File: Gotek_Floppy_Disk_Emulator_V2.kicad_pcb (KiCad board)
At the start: 2 copper layers, 90 x 60 mm, 66 parts, among them J1 Power Connector, J2 OLED Display 0.91" Module, J3 USB_A, J5 Programming Connector, J6 Floppy Data Connector, Q1 MMBT2222, Q2 BSS123, Q3 BSS123, Q4 BSS123, Q5 BSS123, Q6 BSS123, Q7 BSS123, SW1 KY040 Rotary Encoder Module, SW2 DIP Switch, U1 AMS1117-3.3, U2 STM32F105RBTx, U3 STMPS2141, U4 74HCT04, Y1 8MHz

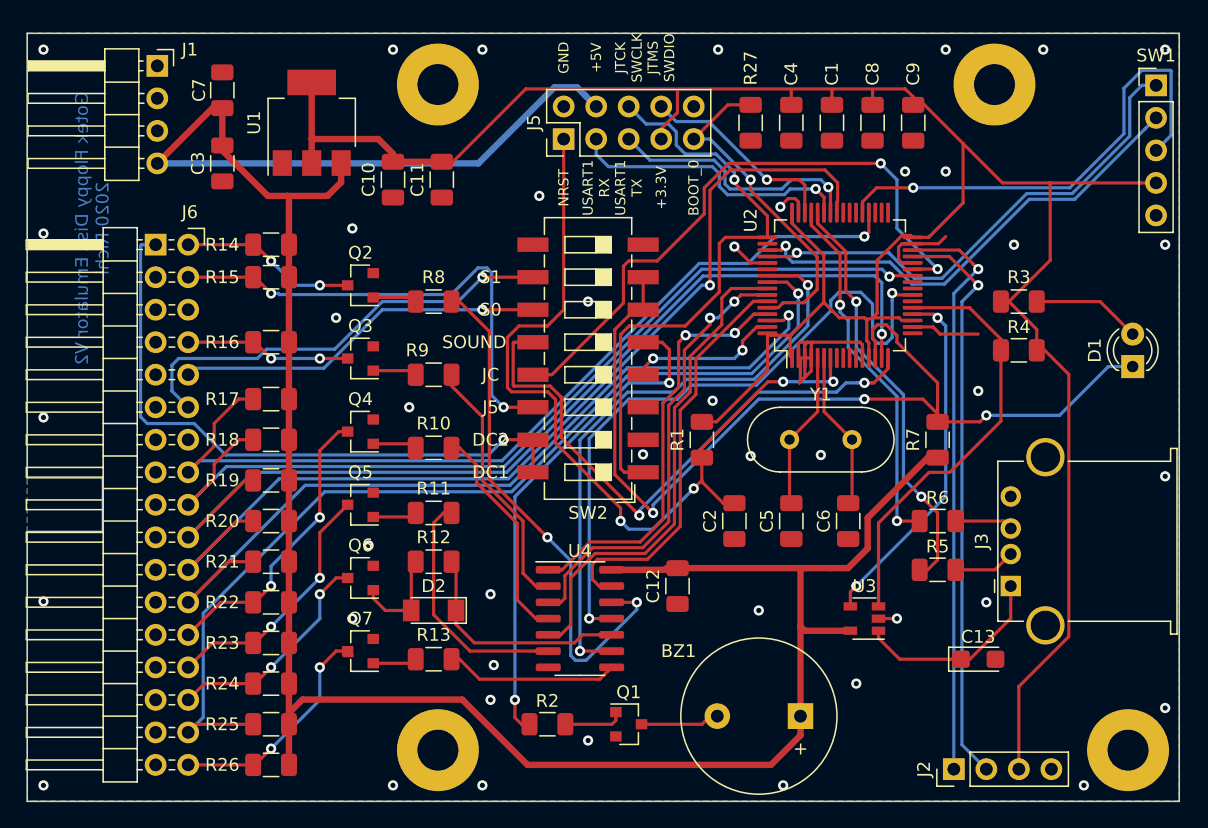
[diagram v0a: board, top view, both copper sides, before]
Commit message: Production files generated
Some parts were exchanged for SMD mounted. For production generation was used Bouni/kicad-jlcpcb-tools plugin.
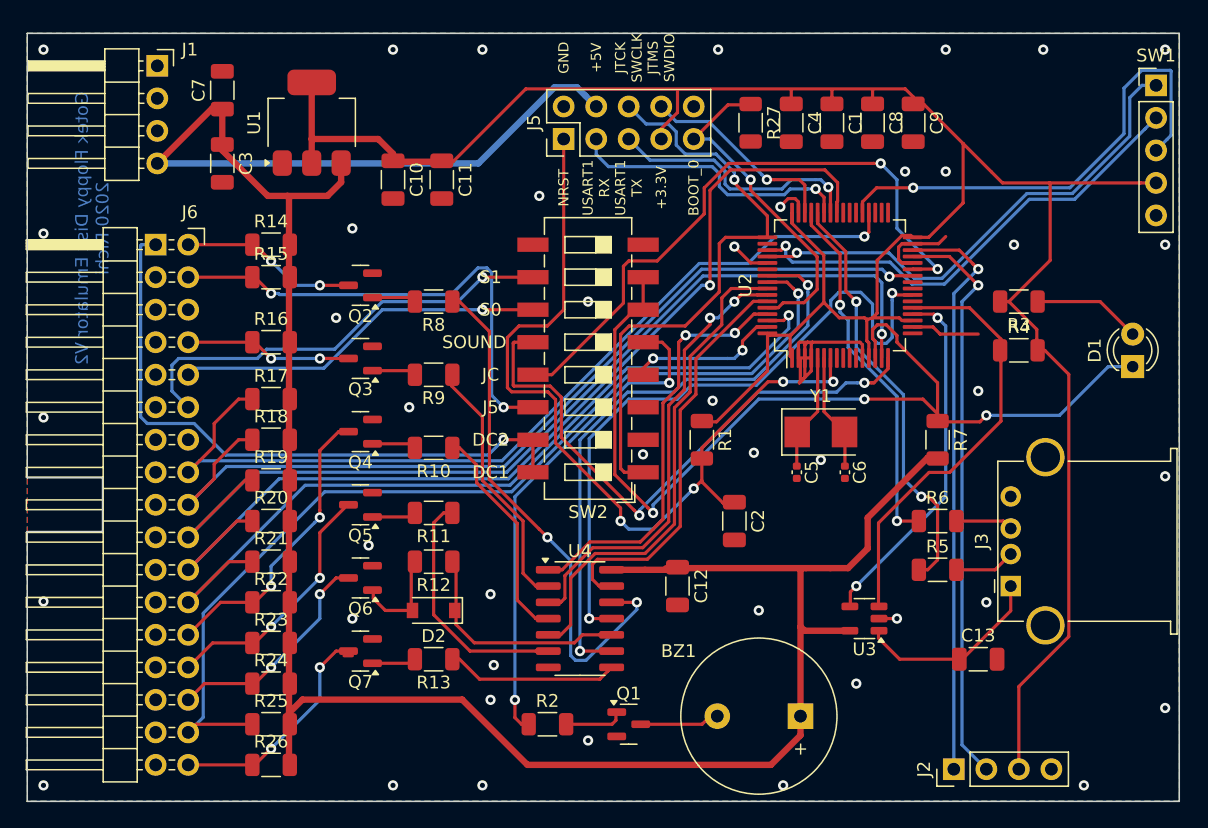
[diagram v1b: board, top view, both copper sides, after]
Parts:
- removed REF** (x4): MountingHole_3.2mm_M3_Pad, Gotek_Floppy_Disk_Emulator_V2:MountingHole_3.2mm_M3_Pad
- C1, C10, C11, C12, C2, C3, C4, C7, C8, C9: footprint Gotek_Floppy_Disk_Emulator_V2:C_1206_3216Metric -> Capacitor_SMD:C_1206_3216Metric
- C13: footprint Gotek_Floppy_Disk_Emulator_V2:CP_EIA-3216-18_Kemet-A -> Capacitor_SMD:C_1206_3216Metric
- C5, C6: footprint Gotek_Floppy_Disk_Emulator_V2:C_1206_3216Metric -> Capacitor_SMD:C_0402_1005Metric
- D1: footprint Gotek_Floppy_Disk_Emulator_V2:LED_D3.0mm -> LED_THT:LED_D3.0mm
- D2: footprint Gotek_Floppy_Disk_Emulator_V2:D_MiniMELF -> Diode_SMD:D_SOD-123
- J5: footprint Gotek_Floppy_Disk_Emulator_V2:PinHeader_2x05_P2.54mm_Vertical -> Connector_PinHeader_2.54mm:PinHeader_2x05_P2.54mm_Vertical
- Q1, Q2, Q3, Q4, Q5, Q6, Q7: footprint Gotek_Floppy_Disk_Emulator_V2:SOT-23 -> Package_TO_SOT_SMD:SOT-23
- R1, R10, R11, R12, R13, R14, R15, R16, R17, R18, R19, R2, R20, R21, R22, R23, R24, R25, R26, R27, R3, R4, R5, R6, R7, R8, R9: footprint Gotek_Floppy_Disk_Emulator_V2:R_1206_3216Metric -> Resistor_SMD:R_1206_3216Metric
- SW1: footprint Gotek_Floppy_Disk_Emulator_V2:PinHeader_1x05_P2.54mm_Vertical -> Connector_PinHeader_2.54mm:PinHeader_1x05_P2.54mm_Vertical
- SW2: footprint Gotek_Floppy_Disk_Emulator_V2:SW_DIP_SPSTx08_Slide_6.7x21.88mm_W8.61mm_P2.54mm_LowProfile -> Button_Switch_SMD:SW_DIP_SPSTx08_Slide_6.7x21.88mm_W8.61mm_P2.54mm_LowProfile
- U1: footprint Gotek_Floppy_Disk_Emulator_V2:SOT-223-3_TabPin2 -> Package_TO_SOT_SMD:SOT-223-3_TabPin2
- U3: footprint Gotek_Floppy_Disk_Emulator_V2:SOT-23-5 -> Package_TO_SOT_SMD:SOT-23-5
- U4: footprint Gotek_Floppy_Disk_Emulator_V2:SOIC-14_3.9x8.7mm_P1.27mm -> Package_SO:SOIC-14_3.9x8.7mm_P1.27mm
- Y1: footprint Gotek_Floppy_Disk_Emulator_V2:Crystal_HC49-4H_Vertical -> Crystal:Crystal_SMD_5032-2Pin_5.0x3.2mm
- moved C5 3.83 mm to (142.0, 90.2)
- moved C6 3.82 mm to (145.8, 90.2)
- moved Y1 2.52 mm to (143.9, 87.0)
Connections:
- J1 pad 1: Net-(J1-Pad1) -> unconnected-(J1-Pin_1-Pad1)
- J5 pad 10: Net-(J5-Pad10) -> unconnected-(J5-Pin_10-Pad10)
- J6 pad 14: Net-(J6-Pad14) -> unconnected-(J6-Pin_14-Pad14)
- J6 pad 6: Net-(J6-Pad6) -> unconnected-(J6-Pin_6-Pad6)
- SW2 pad 8: Net-(SW2-Pad8) -> unconnected-(SW2-Pad8)
- SW2 pad 9: Net-(SW2-Pad9) -> unconnected-(SW2-Pad9)
- U2 pad 10: Net-(U2-Pad10) -> unconnected-(U2-PC2-Pad10)
- U2 pad 11: Net-(U2-Pad11) -> unconnected-(U2-PC3-Pad11)
- U2 pad 17: Net-(U2-Pad17) -> unconnected-(U2-PA3-Pad17)
- U2 pad 22: Net-(U2-Pad22) -> unconnected-(U2-PA6-Pad22)
- U2 pad 24: Net-(U2-Pad24) -> unconnected-(U2-PC4-Pad24)
- U2 pad 25: Net-(U2-Pad25) -> unconnected-(U2-PC5-Pad25)
- U2 pad 33: Net-(U2-Pad33) -> unconnected-(U2-PB12-Pad33)
- U2 pad 34: Net-(U2-Pad34) -> unconnected-(U2-PB13-Pad34)
- U2 pad 35: Net-(U2-Pad35) -> unconnected-(U2-PB14-Pad35)
- U2 pad 38: Net-(U2-Pad38) -> unconnected-(U2-PC7-Pad38)
- U2 pad 39: Net-(U2-Pad39) -> unconnected-(U2-PC8-Pad39)
- U2 pad 40: Net-(U2-Pad40) -> unconnected-(U2-PC9-Pad40)
- U2 pad 50: Net-(U2-Pad50) -> unconnected-(U2-PA15-Pad50)
- U2 pad 54: Net-(U2-Pad54) -> unconnected-(U2-PD2-Pad54)
- U2 pad 8: Net-(U2-Pad8) -> unconnected-(U2-PC0-Pad8)
- U2 pad 9: Net-(U2-Pad9) -> unconnected-(U2-PC1-Pad9)
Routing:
- net Net-(U2-PD1): track 12.4 -> 9.97 mm
- net Net-(U2-PD0): track 12.3 -> 9.97 mm
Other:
- net class Default removed
- net class Power removed

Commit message: V2.1
Production files for JLCPCB excluding through hole parts and 8bit switch. Capacitors moved close to the voltage input pins of the MCU.
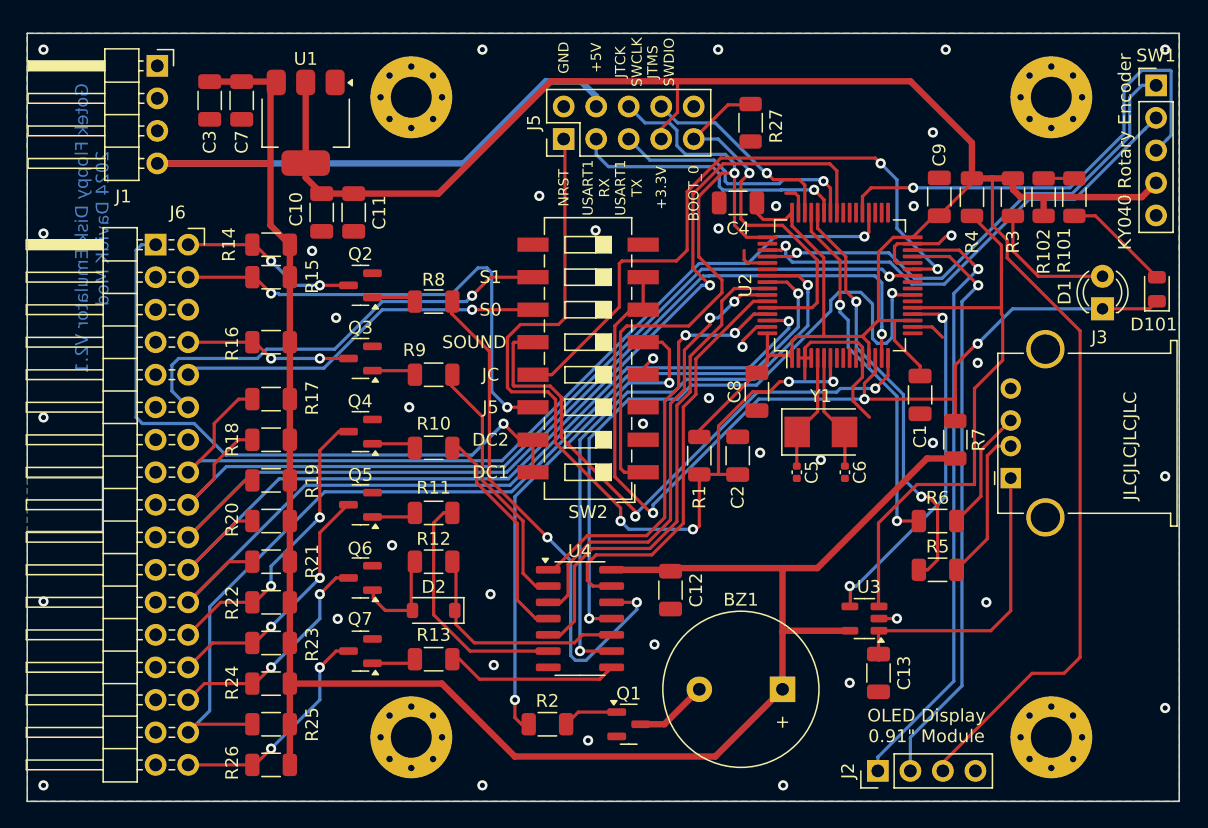
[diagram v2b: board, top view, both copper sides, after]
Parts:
- added D101: LED Green, LED_SMD:LED_0805_2012Metric, F.Cu at (170.2, 75.9)
- added H1: Hole1, MountingHole:MountingHole_3.2mm_M3_Pad_Via, F.Cu at (161.9, 60.9)
- added H2: Hole2, MountingHole:MountingHole_3.2mm_M3_Pad_Via, F.Cu at (161.9, 110.9)
- added H3: Hole3, MountingHole:MountingHole_3.2mm_M3_Pad_Via, F.Cu at (111.9, 60.9)
- added H4: Hole4, MountingHole:MountingHole_3.2mm_M3_Pad_Via, F.Cu at (111.9, 110.9)
- added R101: 1K, Resistor_SMD:R_1206_3216Metric, F.Cu at (163.7, 68.7)
- added R102: 1K, Resistor_SMD:R_1206_3216Metric, F.Cu at (161.3, 68.7)
- C13: value 4.7uF/16V -> 10uF/16V
- SW1: value KY040 Rotary Encoder Module -> KY040 Rotary Encoder
- moved C8 22.9 mm to (138.9, 83.9)
- moved C1 22.3 mm to (151.7, 84.1)
- moved R4 12.5 mm to (155.7, 68.7), turned to 90 degrees
- moved J3 8.44 mm to (158.8, 90.6)
- moved R3 8.17 mm to (158.9, 68.7), turned to 90 degrees
- moved C13 7.86 mm to (148.4, 105.8), turned to -90 degrees
- moved C4 7.52 mm to (137.4, 69.1), turned to 180 degrees
- moved C11 7.34 mm to (107.4, 69.9)
- moved C9 6.13 mm to (153.2, 68.6), turned to 90 degrees
- moved C10 6.13 mm to (104.9, 69.9)
- moved J2 5.94 mm to (148.4, 113.5)
- moved C2 5.11 mm to (137.4, 88.9), turned to 90 degrees
- moved D1 5.09 mm to (165.9, 77.4)
- moved C3 5.01 mm to (96.2, 61.1)
- moved BZ1 2.52 mm to (140.9, 107.1)
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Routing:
- net +3V3: track 192.4 -> 207.1 mm
- net GNDD: track 48.1 -> 35.1 mm, vias 45 -> 40
- net Net-(U2-PA5): track 33.7 -> 45.1 mm
- net Net-(D101-A): track 0.00 -> 8.44 mm
- net Net-(J3-VBUS): track 15.1 -> 23.2 mm
- net Net-(J3-D-): track 4.82 -> 12.1 mm
- net JTCK-SWCLK: track 46.3 -> 52.2 mm
- net Net-(J3-D+): track 4.56 -> 9.62 mm
- net FPI5V_DSELn: track 78.1 -> 74.7 mm
- net BOOT_0: track 26.5 -> 29.7 mm
- net +5V: track 197.6 -> 194.9 mm
- net Net-(J2-SDA): track 45.6 -> 48.2 mm
- net FPI5V_WDATAn: track 77.5 -> 80.0 mm
- net Net-(R101-Pad2): track 0.00 -> 2.40 mm
- net JUMPER_JC: track 48.9 -> 51.1 mm
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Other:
- board text added: "Gotek Floppy Disk Emulator V2.1 2024 DavidK Mod"
- board text added: "JLCJLCJLCJLC"
- board text added: "OLED Display 0.91{dblquote} Module"
- board text removed: "Gotek Floppy Disk Emulator V2 2020 Richi"

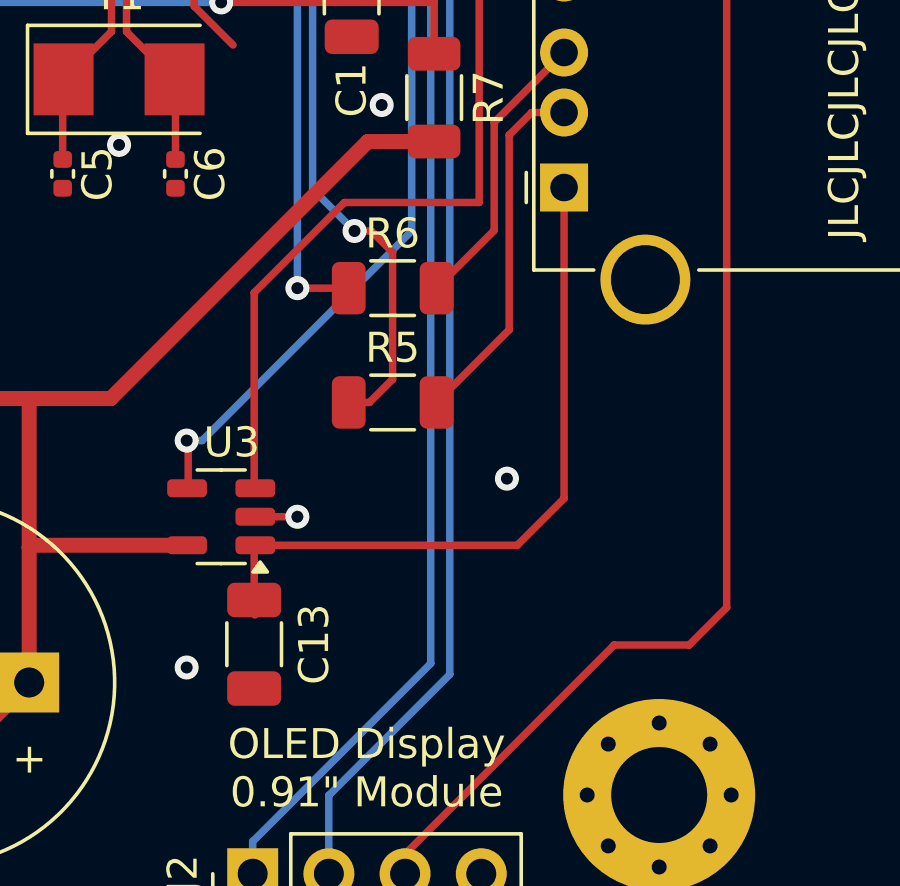
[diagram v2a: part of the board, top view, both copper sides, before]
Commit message: Wider 5V patch for USB
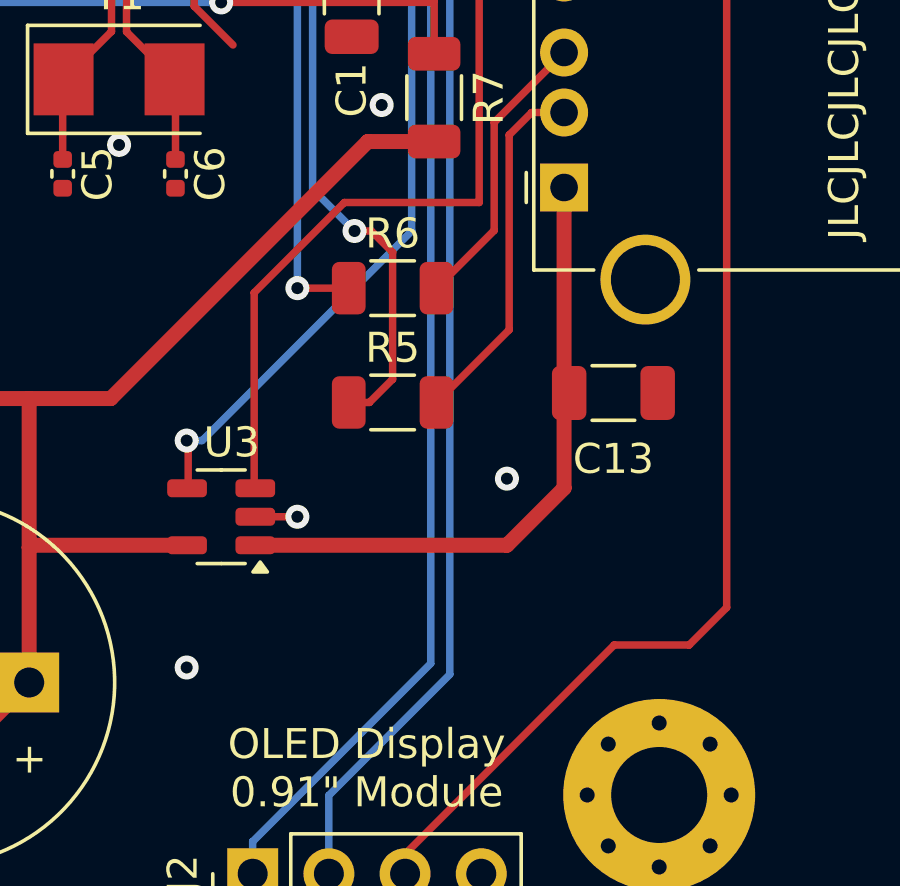
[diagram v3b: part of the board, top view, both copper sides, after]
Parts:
- moved C13 14.6 mm to (160.4, 97.5), turned to 0 degrees
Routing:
- net Net-(J3-VBUS): track 23.2 -> 21.1 mm
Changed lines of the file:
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@@
 		(tags "capacitor")
 		(property "Reference" "C2"
-			(at -3.25 0 270)
+			(at -3.25 0 -90)
 			(layer "F.SilkS")
 			(effects
@@
 		)
 		(property "Value" "100nF"
-			(at 0 1.85 270)
+			(at 0 1.85 -90)
 			(layer "F.Fab")
 			(effects
@@
 		)
 		(fp_text user "${REFERENCE}"
-			(at 0 0 270)
+			(at 0 0 -90)
 			(layer "F.Fab")
 			(effects
@@
 		)
 		(property "Value" "100nF"
-			(at 0 1.85 270)
+			(at 0 1.85 -90)
 			(layer "F.Fab")
 			(effects
@@
 		)
 		(fp_text user "${REFERENCE}"
-			(at 0 0 270)
+			(at 0 0 -90)
 			(layer "F.Fab")
 			(effects
@@
 	(footprint "Capacitor_SMD:C_1206_3216Metric"
 		(layer "F.Cu")
-		(at 148.4199 105.8498 -90)
+		(at 160.3949 97.4748)
 		(descr "Capacitor SMD 1206 (3216 Metric), square (rectangular) end terminal, IPC_7351 nominal, (Body size source: IPC-SM-782 page 76, https://www.pcb-3d.com/wordpress/wp-content/uploads/ipc-sm-782a_amendment_1_and_2.pdf), generated with kicad-footprint-generator")
 		(tags "capacitor")
 		(property "Reference" "C13"
-			(at 0 -2 -90)
+			(at 0 2.2 0)
 			(layer "F.SilkS")
 			(effects
@@
 		)
 		(property "Value" "10uF/16V"
-			(at 0 1.85 90)
+			(at 0 1.85 360)
 			(layer "F.Fab")
 			(effects
@@
 		)
 		(property "Footprint" "Capacitor_SMD:C_1206_3216Metric"
-			(at 0 0 -90)
+			(at 0 0 0)
 			(unlocked yes)
 			(layer "F.Fab")
@@
 		)
 		(property "Datasheet" ""
-			(at 0 0 -90)
+			(at 0 0 0)
 			(unlocked yes)
 			(layer "F.Fab")
@@
 		)
 		(property "Description" ""
-			(at 0 0 -90)
+			(at 0 0 0)
 			(unlocked yes)
 			(layer "F.Fab")
@@
 		(attr smd)
 		(fp_line
-			(start -0.711252 0.91)
-			(end 0.711252 0.91)
+			(start -0.711252 -0.91)
+			(end 0.711252 -0.91)
 			(stroke
 				(width 0.12)
@@
 		)
 		(fp_line
-			(start -0.711252 -0.91)
-			(end 0.711252 -0.91)
+			(start -0.711252 0.91)
+			(end 0.711252 0.91)
 			(stroke
 				(width 0.12)
@@
 		)
 		(fp_line
-			(start -2.3 1.15)
-			(end -2.3 -1.15)
+			(start -2.3 -1.15)
+			(end 2.3 -1.15)
 			(stroke
 				(width 0.05)
@@
 		)
 		(fp_line
-			(start 2.3 1.15)
-			(end -2.3 1.15)
+			(start -2.3 1.15)
+			(end -2.3 -1.15)
 			(stroke
 				(width 0.05)
@@
 		)
 		(fp_line
-			(start -2.3 -1.15)
-			(end 2.3 -1.15)
+			(start 2.3 -1.15)
+			(end 2.3 1.15)
 			(stroke
 				(width 0.05)
@@
 		)
 		(fp_line
-			(start 2.3 -1.15)
-			(end 2.3 1.15)
+			(start 2.3 1.15)
+			(end -2.3 1.15)
 			(stroke
 				(width 0.05)
@@
 		)
 		(fp_line
-			(start -1.6 0.8)
-			(end -1.6 -0.8)
+			(start -1.6 -0.8)
+			(end 1.6 -0.8)
 			(stroke
 				(width 0.1)
@@
 		)
 		(fp_line
-			(start 1.6 0.8)
-			(end -1.6 0.8)
+			(start -1.6 0.8)
+			(end -1.6 -0.8)
 			(stroke
 				(width 0.1)
@@
 		)
 		(fp_line
-			(start -1.6 -0.8)
-			(end 1.6 -0.8)
+			(start 1.6 -0.8)
+			(end 1.6 0.8)
 			(stroke
 				(width 0.1)
@@
 		)
 		(fp_line
-			(start 1.6 -0.8)
-			(end 1.6 0.8)
+			(start 1.6 0.8)
+			(end -1.6 0.8)
 			(stroke
 				(width 0.1)
@@
 		)
 		(fp_text user "${REFERENCE}"
-			(at 0 0 90)
+			(at 0 0 360)
 			(layer "F.Fab")
 			(effects
@@
 		)
 		(pad "1" smd roundrect
-			(at -1.475 0 270)
+			(at -1.475 0)
 			(size 1.15 1.8)
 			(layers "F.Cu" "F.Paste" "F.Mask")
@@
 		)
 		(pad "2" smd roundrect
-			(at 1.475 0 270)
+			(at 1.475 0)
 			(size 1.15 1.8)
 			(layers "F.Cu" "F.Paste" "F.Mask")
@@
 	)
 	(segment
-		(start 157.1904 102.55)
-		(end 158.75 100.9904)
-		(width 0.25)
-		(layer "F.Cu")
-		(net 36)
-	)
-	(segment
-		(start 148.4199 102.5876)
-		(end 148.4575 102.55)
-		(width 0.25)
+		(start 158.75 100.6447)
+		(end 158.75 90.6248)
+		(width 0.5)
 		(layer "F.Cu")
 		(net 36)
 	)
 	(segment
-		(start 148.4199 104.3748)
-		(end 148.4199 102.5876)
-		(width 0.25)
+		(start 156.8447 102.55)
+		(end 158.75 100.6447)
+		(width 0.5)
 		(layer "F.Cu")
 		(net 36)
@@
 	(segment
 		(start 148.4575 102.55)
-		(end 157.1904 102.55)
-		(width 0.25)
-		(layer "F.Cu")
-		(net 36)
-	)
-	(segment
-		(start 158.75 90.6248)
-		(end 158.75 100.9904)
-		(width 0.25)
-		(layer "F.Cu")
-		(net 36)
-	)
-	(segment
-		(start 148.4575 104.8622)
-		(end 148.4449 104.8748)
-		(width 0.25)
+		(end 156.8447 102.55)
+		(width 0.5)
 		(layer "F.Cu")
 		(net 36)
